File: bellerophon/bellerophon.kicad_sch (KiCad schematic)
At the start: 23 parts, among them Q1 IRLB8721PBF

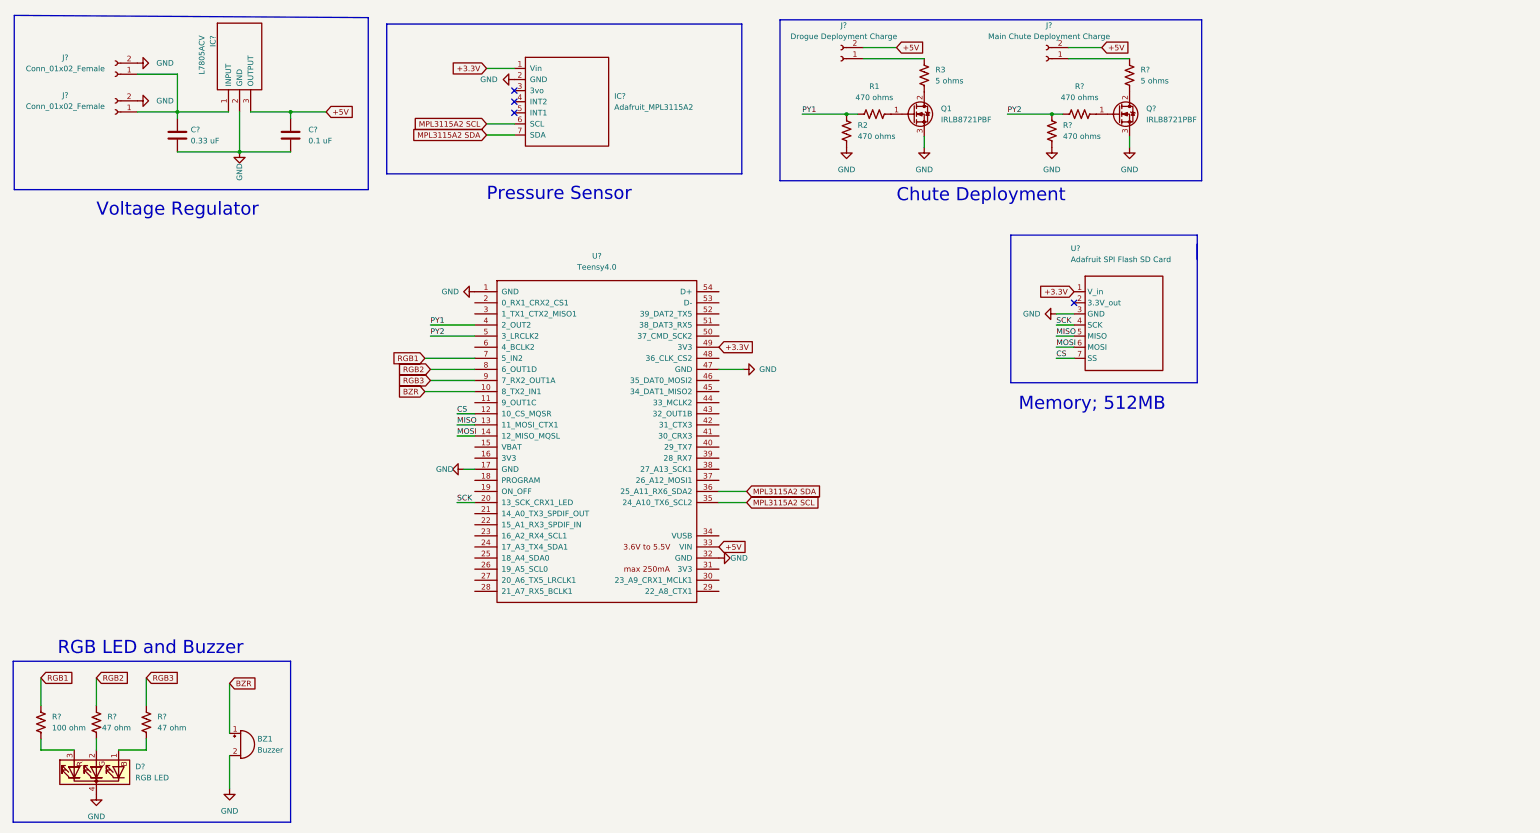
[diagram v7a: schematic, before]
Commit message: Add Adafruit ICM20948 footprint to adafruit library. Also add Adafruit ICM20948 wiring to the schematics file
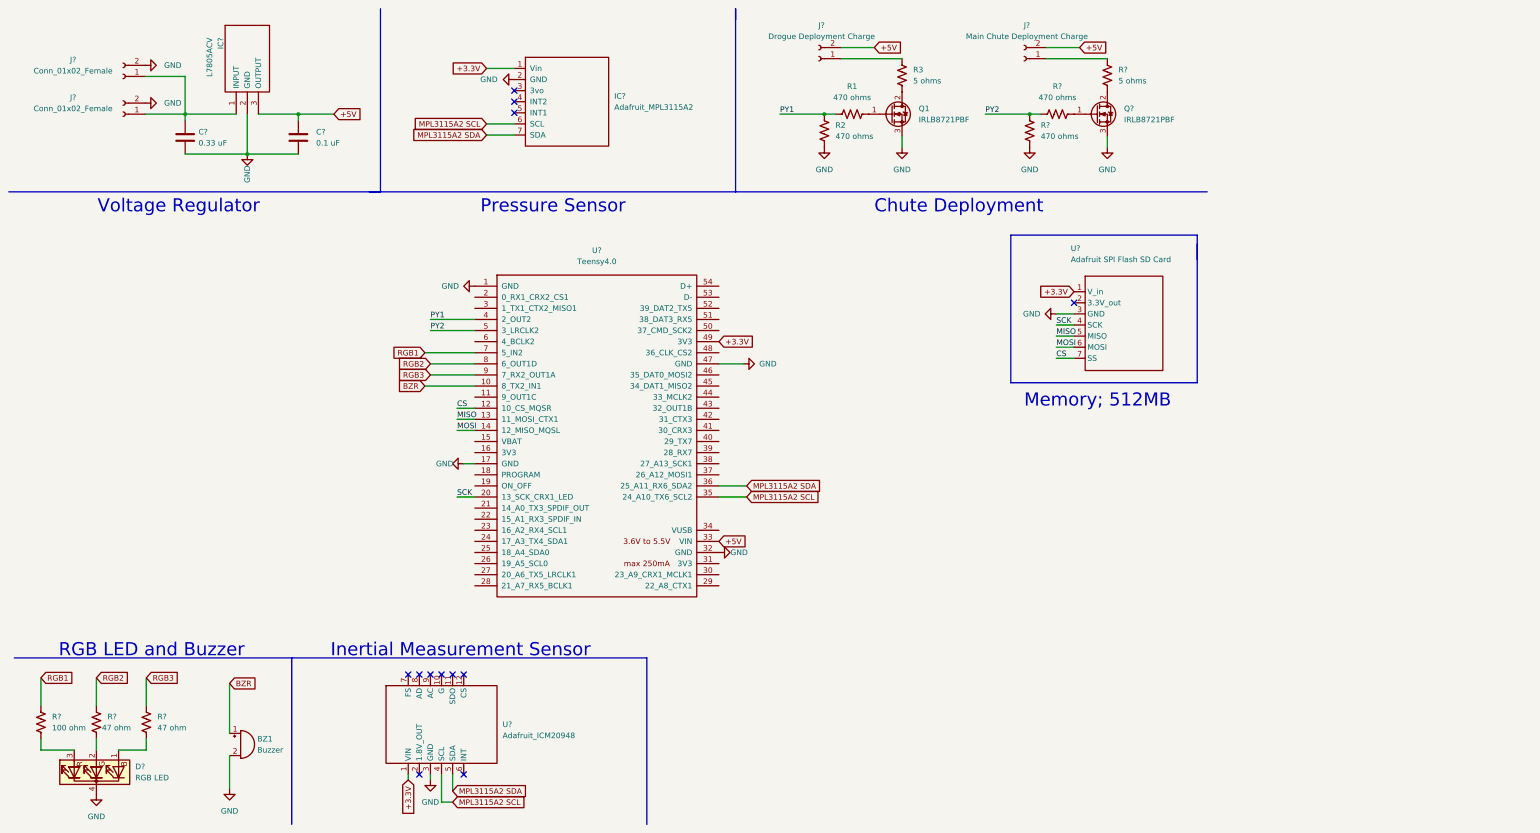
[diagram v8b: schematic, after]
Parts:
- added U?: Adafruit_ICM20948, symbol Adafruit:Adafruit_ICM20948
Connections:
- net +3.3V: now also U?.1 (VIN)
- net GND: now also U?.3 (GND)
- net MPL3115A2 SCL: now also U?.4 (SCL)
- net MPL3115A2 SDA: now also U?.5 (SDA)
- no-connect marks 4 -> 12
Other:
- note added: "Inertial Measurement Sensor"
- moved on the sheet: C?, IC?, J?, Q1, Q?, R1, R2, R3, R?, U?
